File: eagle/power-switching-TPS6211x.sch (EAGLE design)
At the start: 13 parts, among them U1 TPS6211X

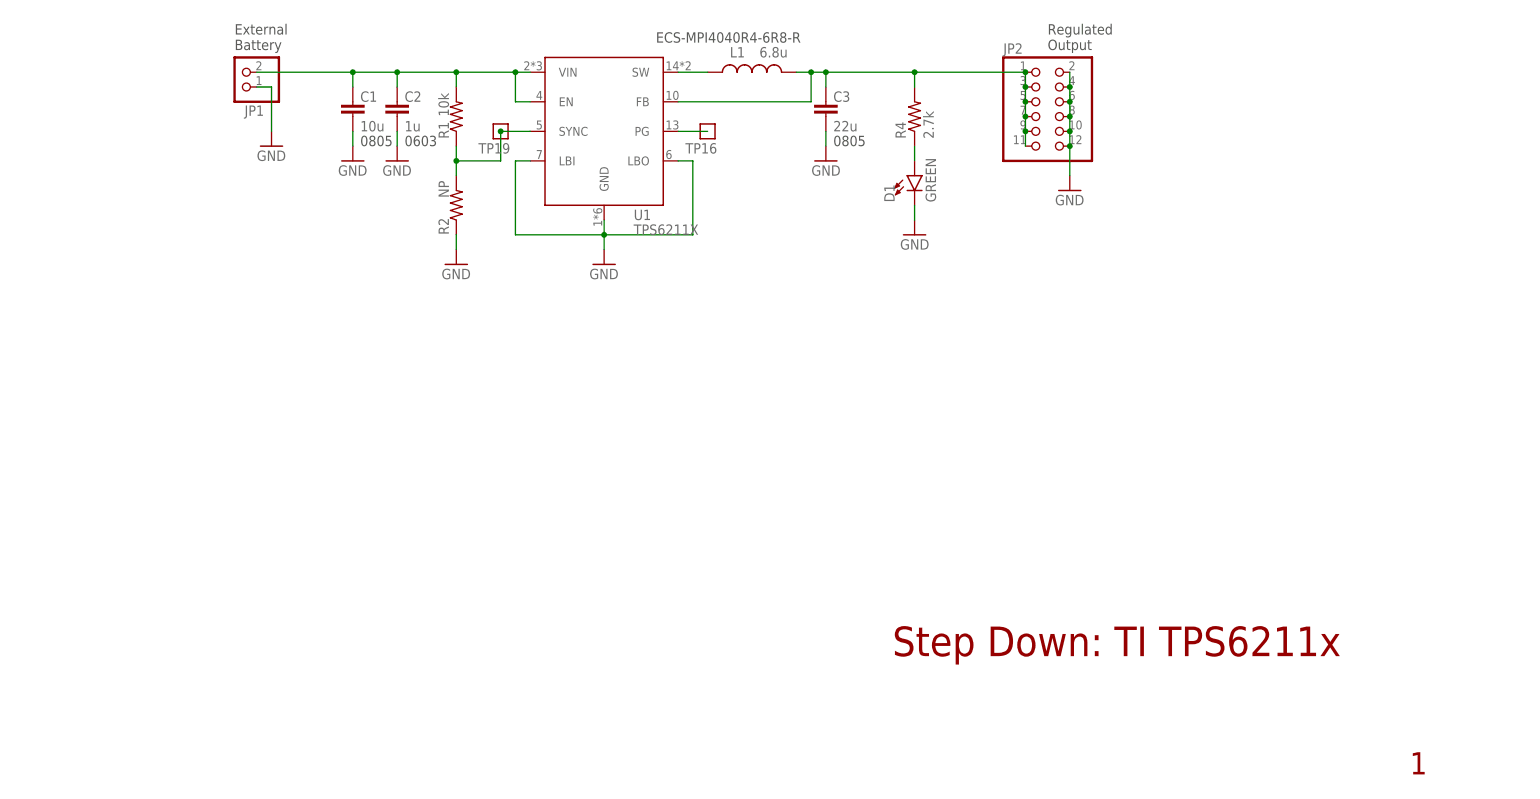
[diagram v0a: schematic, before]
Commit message: Added enable control, and sync options for switching
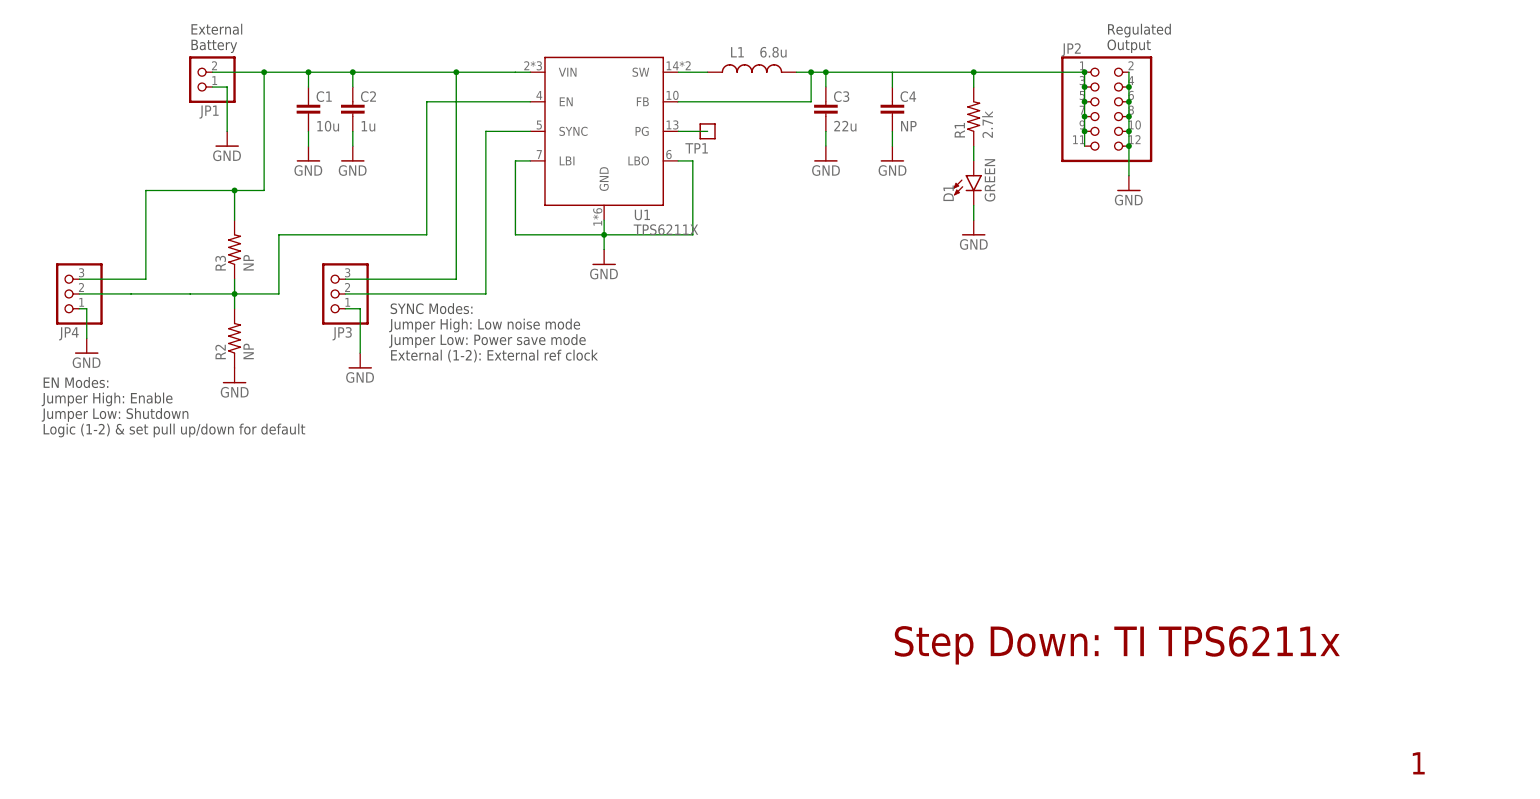
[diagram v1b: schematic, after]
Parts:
- removed R4: 2.7k, rcl_custom:R-US_0402-B-NOSILK
- removed TP19: TEST-POINT, Tova:TEST-POINT
- added C4: NP, oresat-rcl:C-EU0805-B-NOSILK
- added JP3, JP4: (no value), pinhead:PINHD-1X3
- added R3: NP, oresat-rcl:R-US_0603-B-NOSILK
- C2: DIS Digi-Key -> (none); DPN 1276-1001-1-ND -> (none); MFR Samsung -> (none); MPN CL05B104KO5NNNC -> (none)
- R1: value 10k -> 2.7k; device rcl_custom:R-US_0402-B-NOSILK -> oresat-rcl:R-US_0603-B-NOSILK; DIS Digi-Key -> (none); DPN 1276-4275-1-ND -> (none); MFR Samsung -> (none); MPN RC1005F6653CS -> (none)
- R2: device rcl_custom:R-US_0402-B-NOSILK -> oresat-rcl:R-US_0603-B-NOSILK; DIS Digi-Key -> (none); DPN 1276-4275-1-ND -> (none); MFR Samsung -> (none); MPN RC1005F6653CS -> (none)
- U1: MFR TI -> (none); MPN TPS62111RSA -> (none)
- renumbered TP16 to TP1
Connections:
- removed net N$80: C1.1, C2.1, JP1.2, R1.2, U1.EN, U1.VIN
- removed net TPS62111-SYNC: R1.1, R2.2, TP19.1, U1.SYNC
- new net N$1: JP3.2, U1.SYNC
- new net N$2: JP4.2, R2.2, R3.1, U1.EN
- new net N$3: C4.1
- new net N$77: C1.1, C2.1, JP1.2, JP3.3, JP4.3, R3.2, U1.VIN
- net GND: now also C4.2, JP3.1, JP4.1
- net N$271: now also R1.1; no longer R4.1
- net N$79: now also R1.2; no longer R4.2
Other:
- note added: "EN Modes: Jumper High: Enable Jumper Low: Shutdown Logic (1-2) & set pull up/down for default"
- note added: "SYNC Modes: Jumper High: Low noise mode Jumper Low: Power save mode External (1-2): External ref clock"
- note removed: "0603"
- note removed: "0805"
- note removed: "ECS-MPI4040R4-6R8-R"
- moved on the sheet: C1, C2, D1, JP1, JP2, R1, R2

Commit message: Finish TPS6211x layout
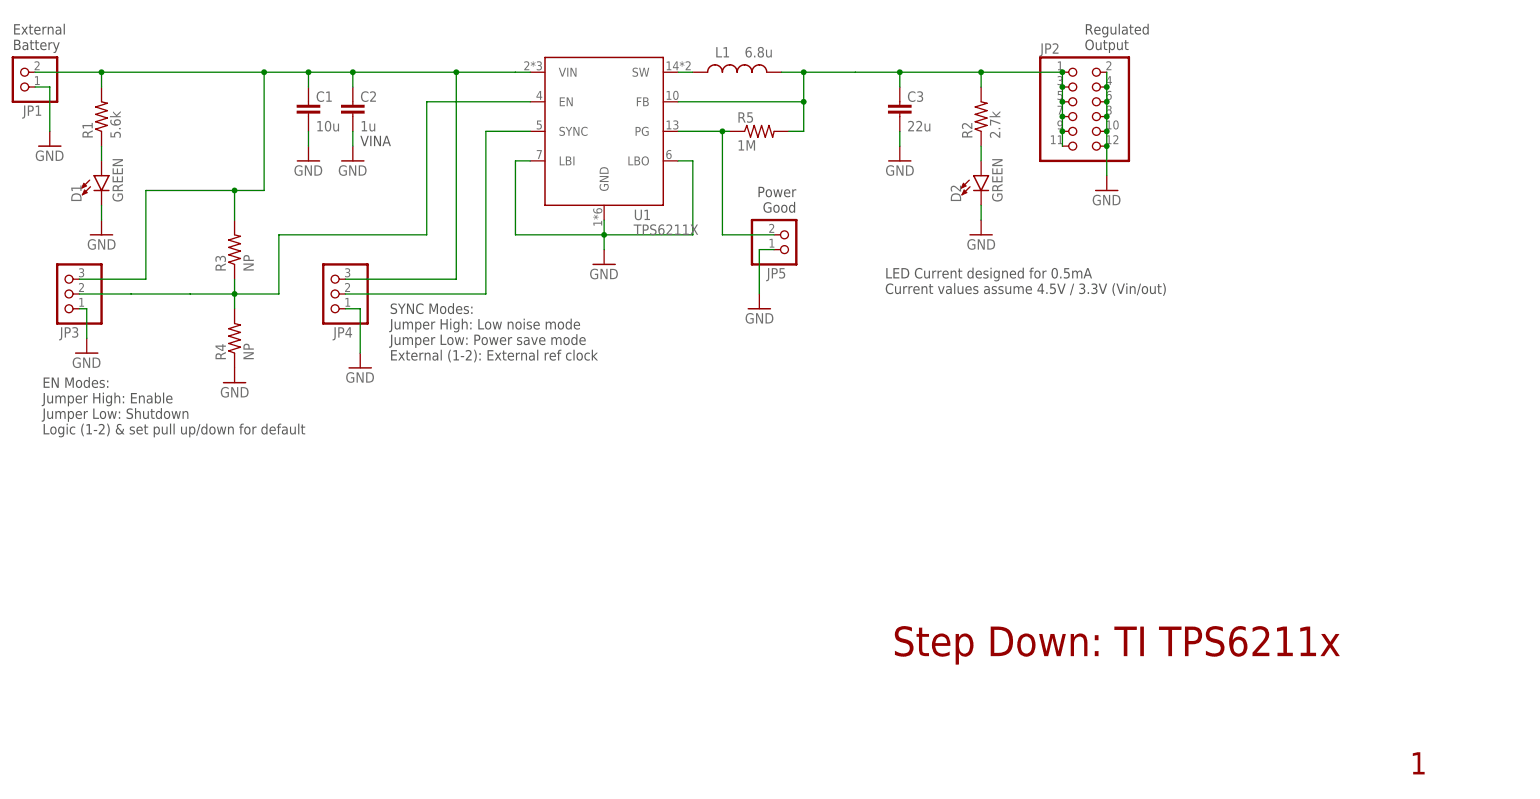
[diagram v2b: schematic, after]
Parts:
- removed C4: NP, oresat-rcl:C-EU0805-B-NOSILK
- removed TP1: TEST-POINT, Tova:TEST-POINT
- added D2: GREEN, SparkFun-LED:LED-GREEN0603
- added JP5: (no value), pinhead:PINHD-1X2
- added R4: NP, oresat-rcl:R-US_0603-B-NOSILK
- added R5: 1M, oresat-rcl:R-US_0402-B-NOSILK
- C1, C3: device oresat-rcl:C-EU0805-B-NOSILK -> oresat-rcl:C-EU1206-B
- R1: value 2.7k -> 5.6k
- R2: value NP -> 2.7k
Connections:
- net TPS62111_SW renamed SW
- removed net N$1: JP3.2, U1.SYNC
- removed net N$2: JP4.2, R2.2, R3.1, U1.EN
- removed net N$3: C4.1
- removed net N$77: C1.1, C2.1, JP1.2, JP3.3, JP4.3, R3.2, U1.VIN
- removed net N$79: C3.1, JP2.1, JP2.11, JP2.3, JP2.5, JP2.7, JP2.9, L1.2, R1.2, U1.FB
- removed net TPS62111-PG: TP1.1, U1.PG
- new net +VIN: C1.1, C2.1, JP1.2, JP3.3, JP4.3, R1.2, R3.2, U1.VIN
- new net +VOUT: C3.1, JP2.1, JP2.11, JP2.3, JP2.5, JP2.7, JP2.9, L1.2, R2.2, R5.2, U1.FB
- new net EN: JP3.2, R3.1, R4.2, U1.EN
- new net N$271: D2.A, R2.1
- new net PG: JP5.2, R5.1, U1.PG
- new net SYNC: JP4.2, U1.SYNC
- net GND: now also D2.C, JP5.1, R4.1; no longer C4.2, R2.1
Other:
- note added: "LED Current designed for 0.5mA Current values assume 4.5V / 3.3V (Vin/out)"
- note added: "Power Good"
- note added: "VINA"
- moved on the sheet: C3, D1, JP1, JP2, JP3, JP4, L1, R1, R2

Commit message: Notes for TPS6211x
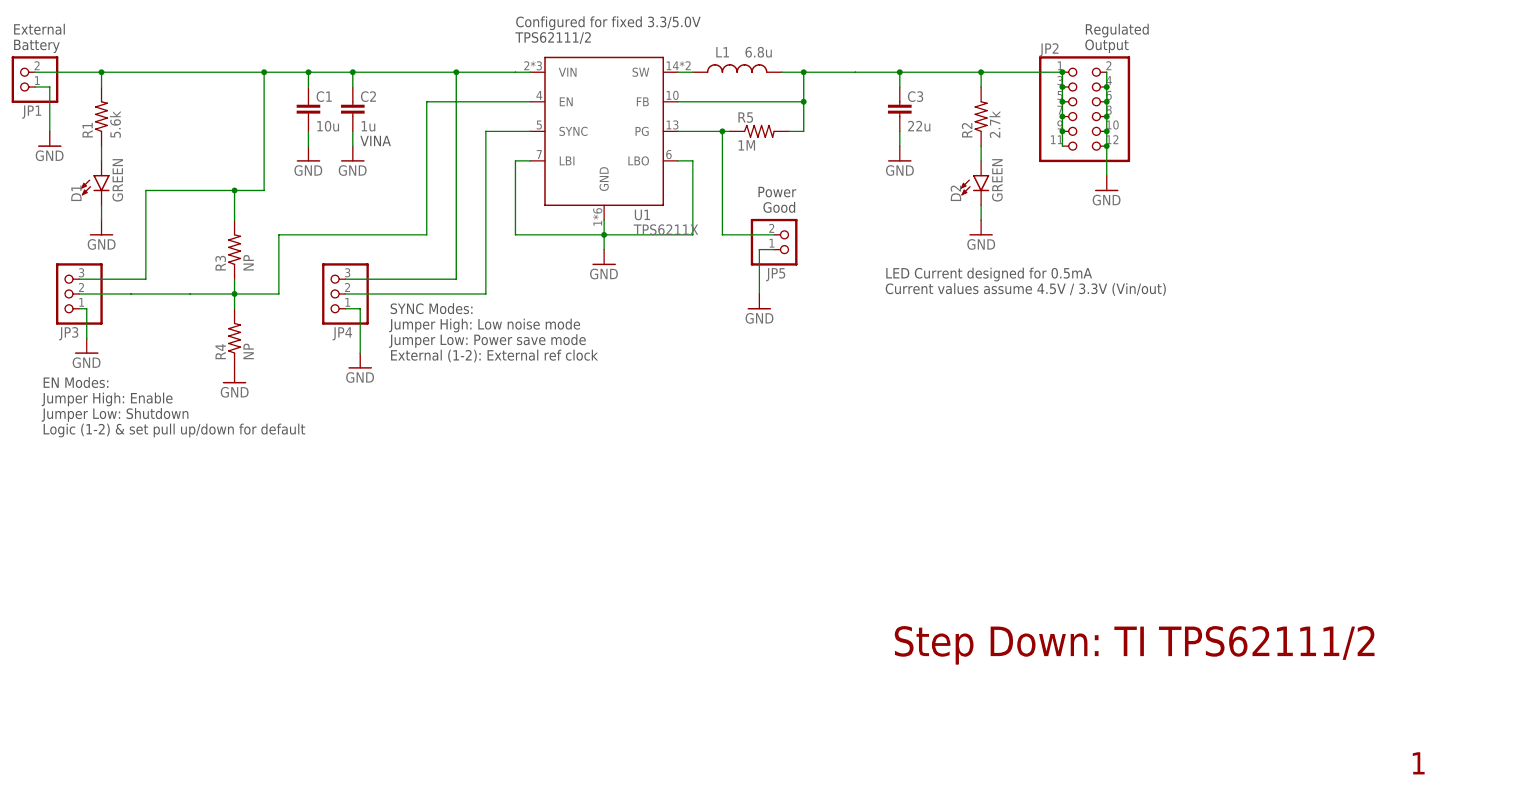
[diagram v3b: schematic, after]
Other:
- note added: "Configured for fixed 3.3/5.0V TPS62111/2"
- note added: "Step Down: TI TPS62111/2"
- note removed: "Step Down: TI TPS6211x"
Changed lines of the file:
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@@
 <sheet>
 <plain>
-<text x="176.53" y="26.67" size="5.08" layer="94">Step Down: TI TPS6211x</text>
+<text x="176.53" y="26.67" size="5.08" layer="94">Step Down: TI TPS62111/2</text>
 <text x="265.43" y="6.35" size="3.81" layer="94">1</text>
 <text x="209.55" y="130.81" size="1.778" layer="97">Regulated
@@
 Current values assume 4.5V / 3.3V (Vin/out)</text>
 <text x="85.09" y="114.3" size="1.778" layer="97">VINA</text>
+<text x="111.76" y="132.08" size="1.778" layer="97">Configured for fixed 3.3/5.0V
+TPS62111/2</text>
 </plain>
 <instances>

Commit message: Add adj and power bad LED for TPS6211x
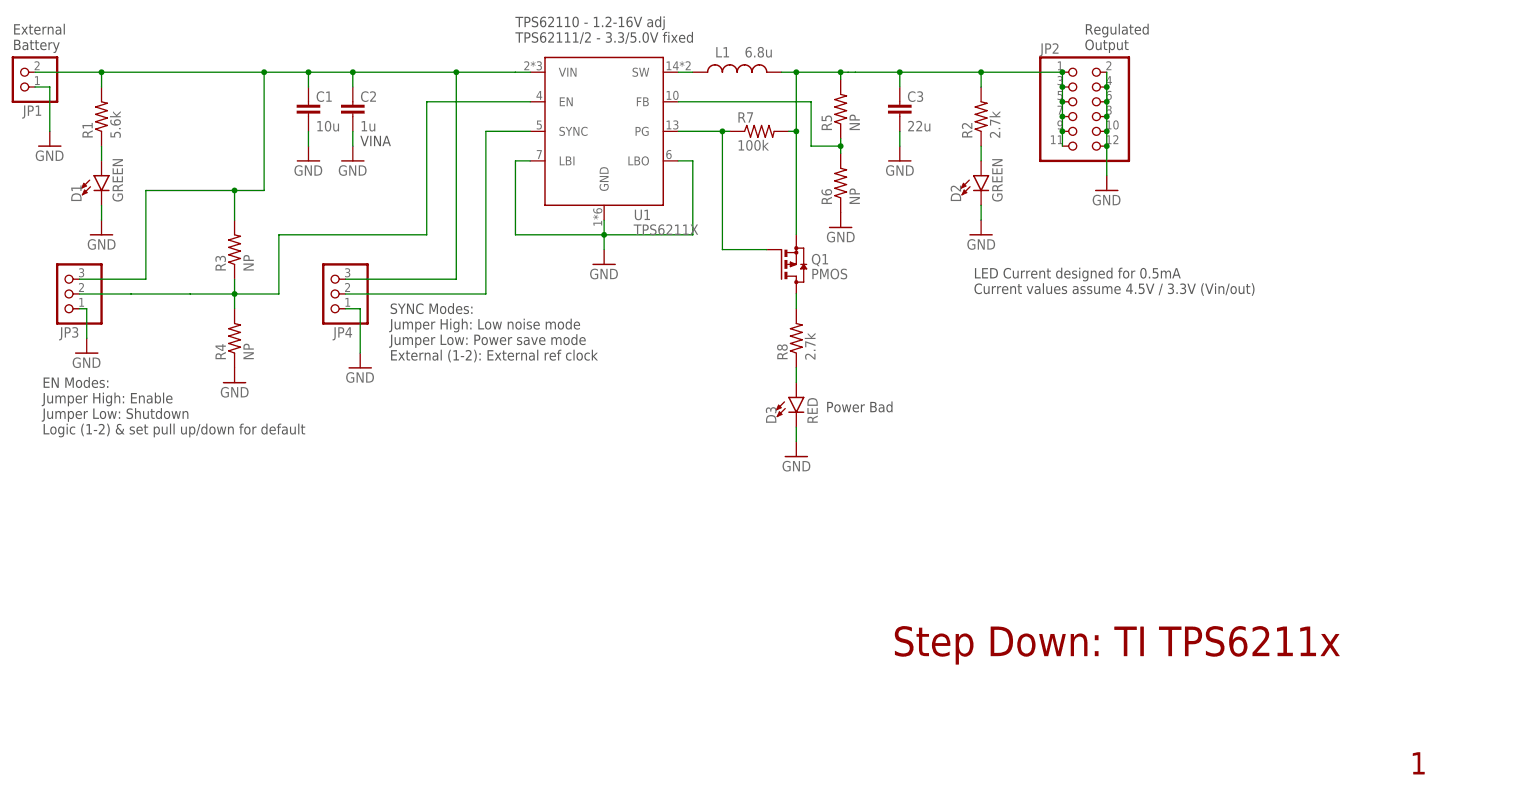
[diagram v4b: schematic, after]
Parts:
- removed JP5: (no value), pinhead:PINHD-1X2
- added D3: RED, SparkFun-LED:LED-GREEN0603
- added Q1: PMOS, transistor-small-signal:BSS84
- added R6: NP, oresat-rcl:R-US_0402-B-NOSILK
- added R7: 100k, oresat-rcl:R-US_0402-B-NOSILK
- added R8: 2.7k, oresat-rcl:R-US_0603-B-NOSILK
- R3, R4: device oresat-rcl:R-US_0603-B-NOSILK -> oresat-rcl:R-US_0402-B-NOSILK
- R5: value 1M -> NP
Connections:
- new net +VOUT1: Q1.D, R8.2
- new net FB: R5.1, R6.2, U1.FB
- new net N$3: D3.A, R8.1
- net +VOUT: now also Q1.S, R7.2; no longer U1.FB
- net GND: now also D3.C, R6.1; no longer JP5.1
- net PG: now also Q1.G, R7.1; no longer JP5.2, R5.1
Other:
- note added: "Power Bad"
- note added: "Step Down: TI TPS6211x"
- note added: "TPS62110 - 1.2-16V adj TPS62111/2 - 3.3/5.0V fixed"
- note removed: "Configured for fixed 3.3/5.0V TPS62111/2"
- note removed: "Power Good"
- note removed: "Step Down: TI TPS62111/2"
- moved on the sheet: R5

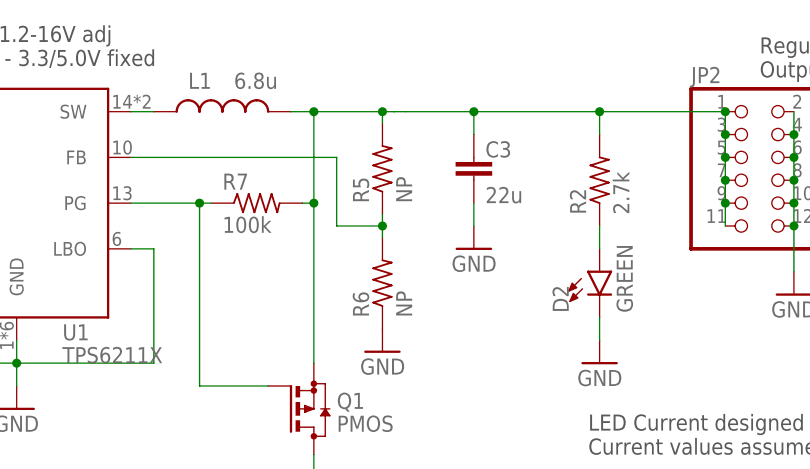
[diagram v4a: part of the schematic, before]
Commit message: Minor fix TPS6211x
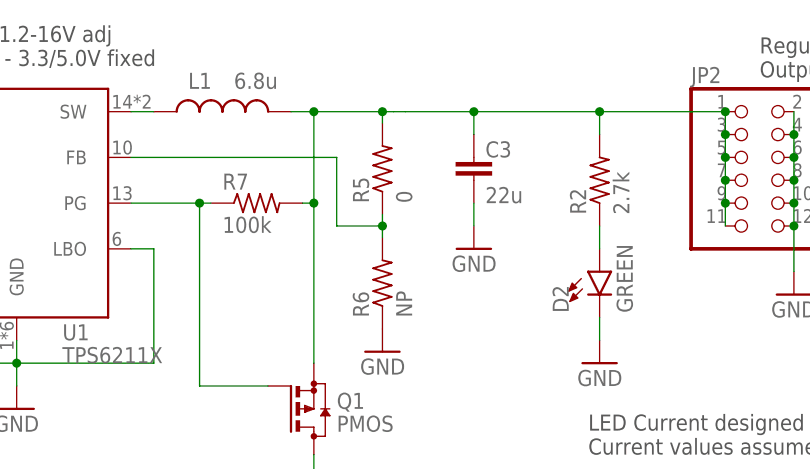
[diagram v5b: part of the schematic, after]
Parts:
- R5: value NP -> 0
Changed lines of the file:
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@@
 <part name="GND6" library="supply1" deviceset="GND" device=""/>
 <part name="R1" library="oresat-rcl" deviceset="R-US_" device="0603-B-NOSILK" value="5.6k"/>
-<part name="R5" library="oresat-rcl" deviceset="R-US_" device="0402-B-NOSILK" value="NP"/>
+<part name="R5" library="oresat-rcl" deviceset="R-US_" device="0402-B-NOSILK" value="0"/>
 <part name="R6" library="oresat-rcl" deviceset="R-US_" device="0402-B-NOSILK" value="NP"/>
 <part name="Q1" library="transistor-small-signal" library_urn="urn:adsk.eagle:library:401" deviceset="BSS84" device="" package3d_urn="urn:adsk.eagle:package:28738/2" value="PMOS"/>

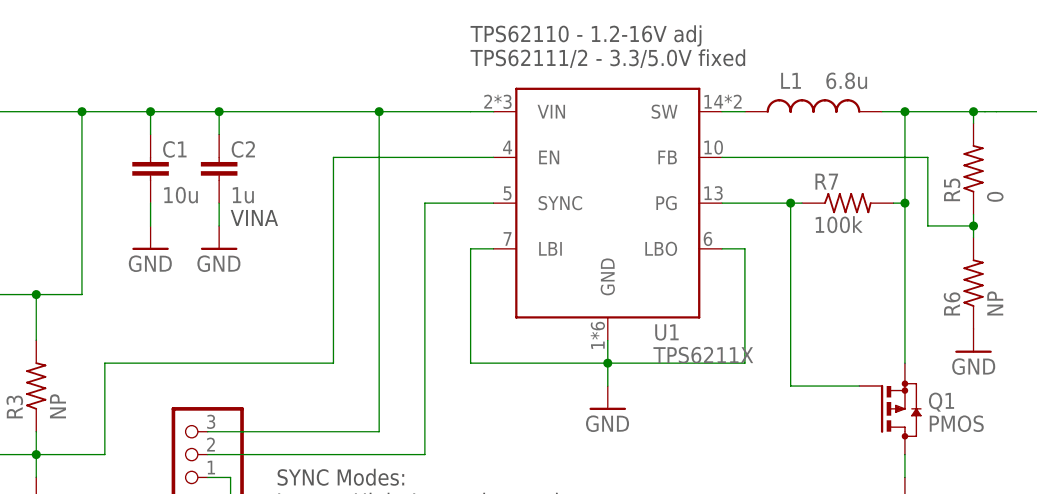
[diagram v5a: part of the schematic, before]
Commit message: TPS6211x - update values
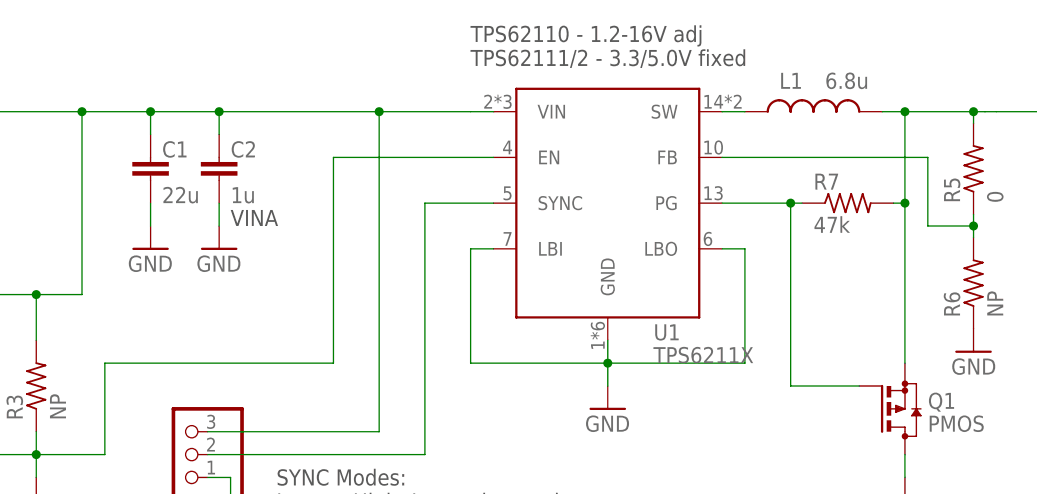
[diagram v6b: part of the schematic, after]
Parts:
- C1: value 10u -> 22u
- R7: value 100k -> 47k
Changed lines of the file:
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@@
 <part name="U1" library="U-TI-TPS6211x-SPS-buck" deviceset="TPS6211X" device="" value="TPS6211X"/>
 <part name="GND39" library="supply1" deviceset="GND" device=""/>
-<part name="C1" library="oresat-rcl" deviceset="C-EU" device="1206-B" value="10u"/>
+<part name="C1" library="oresat-rcl" deviceset="C-EU" device="1206-B" value="22u"/>
 <part name="C2" library="oresat-rcl" deviceset="C-EU" device="0603-B-NOSILK" value="1u"/>
 <part name="GND40" library="supply1" deviceset="GND" device=""/>
@@
 <part name="C3" library="oresat-rcl" deviceset="C-EU" device="1206-B" value="22u"/>
 <part name="R2" library="oresat-rcl" deviceset="R-US_" device="0603-B-NOSILK" value="2.7k"/>
-<part name="R7" library="oresat-rcl" deviceset="R-US_" device="0402-B-NOSILK" value="100k"/>
+<part name="R7" library="oresat-rcl" deviceset="R-US_" device="0402-B-NOSILK" value="47k"/>
 <part name="GND5" library="supply1" deviceset="GND" device=""/>
 <part name="D1" library="SparkFun-LED" library_urn="urn:adsk.eagle:library:529" deviceset="LED-GREEN" device="0603" package3d_urn="urn:adsk.eagle:package:39354/1" value="GREEN">
